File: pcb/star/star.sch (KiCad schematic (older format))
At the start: 20 parts, among them U1 AP2112K-3.3, U2 74AHC595, U3 74AHC595

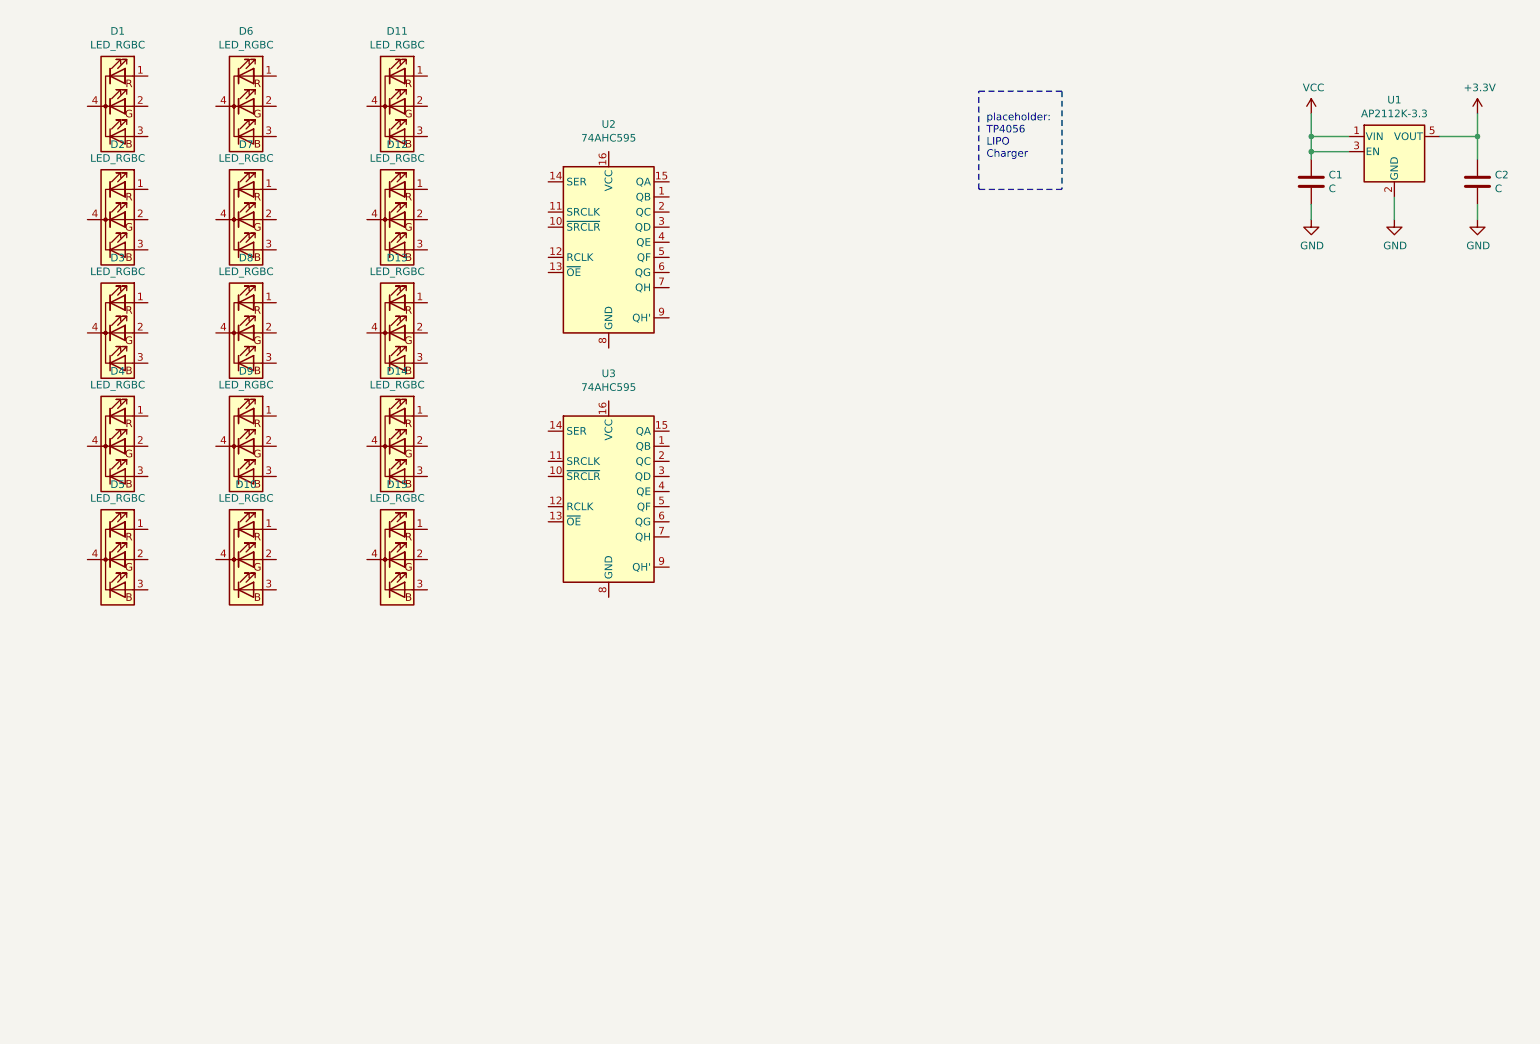
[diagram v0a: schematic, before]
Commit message: apa106 and esp12f used
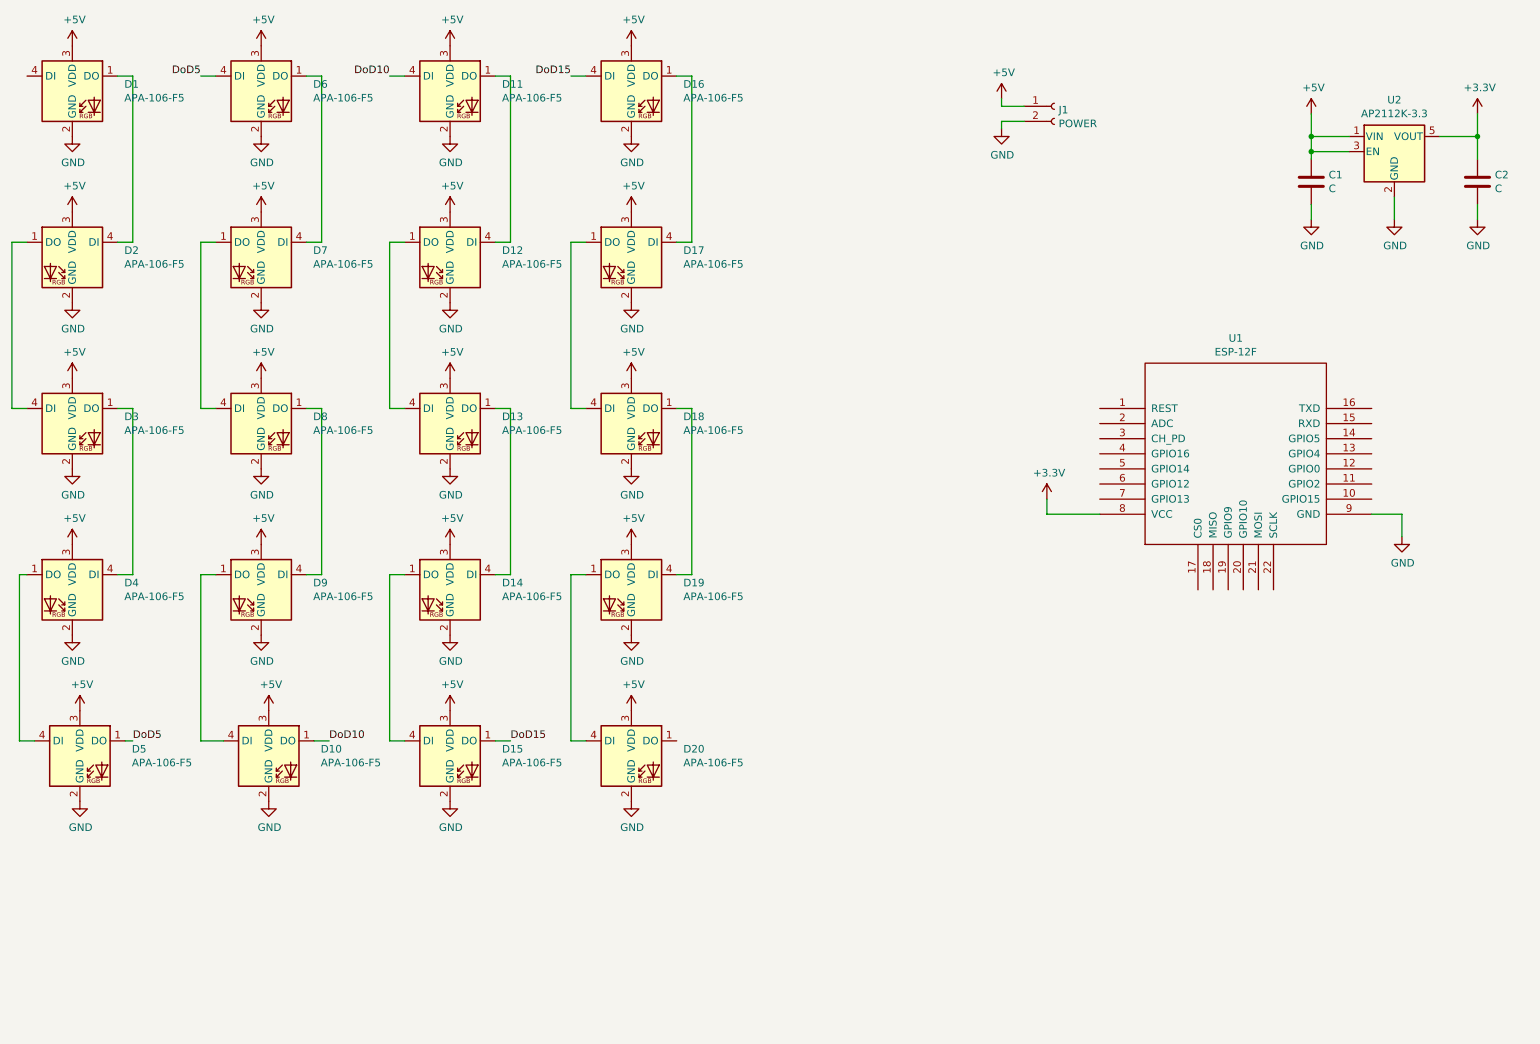
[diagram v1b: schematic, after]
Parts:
- removed D1, D10, D11, D12, D13, D14, D15, D2, D3, D4, D5, D6, D7, D8, D9: LED_RGBC, LED_THT:LED_D5.0mm-4_RGB, symbol Device:LED_RGBC
- removed U2, U3: 74AHC595, Package_SO:SOIC-16_3.9x9.9mm_P1.27mm, symbol 74xx:74AHC595
- added D1, D10, D11, D12, D13, D14, D15, D16, D17, D18, D19, D2, D20, D3, D4, D5, D6, D7, D8, D9: APA-106-F5, LED_THT:LED_D5.0mm-4_RGB, symbol LED:APA-106-F5
- added J1: POWER, Connector_PinSocket_2.54mm:PinSocket_1x02_P2.54mm_Vertical, symbol Connector:Conn_01x02_Female
- added U1: ESP-12F, ESP8266:ESP-12E_SMD, symbol ESP8266:ESP-12F
- renumbered U1 to U2
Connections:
- net +3V3: now also U1.8 (VCC)
- net GND: now also D1.2 (GND), D10.2 (GND), D11.2 (GND), D12.2 (GND), D13.2 (GND), D14.2 (GND), D15.2 (GND), D16.2 (GND), D17.2 (GND), D18.2 (GND), D19.2 (GND), D2.2 (GND), D20.2 (GND), D3.2 (GND), D4.2 (GND), D5.2 (GND), D6.2 (GND), D7.2 (GND), D8.2 (GND), D9.2 (GND), J1.2 (Pin_2), U1.9 (GND)
- net VCC renamed +5V
- net +5V: now also D1.3 (VDD), D10.3 (VDD), D11.3 (VDD), D12.3 (VDD), D13.3 (VDD), D14.3 (VDD), D15.3 (VDD), D16.3 (VDD), D17.3 (VDD), D18.3 (VDD), D19.3 (VDD), D2.3 (VDD), D20.3 (VDD), D3.3 (VDD), D4.3 (VDD), D5.3 (VDD), D6.3 (VDD), D7.3 (VDD), D8.3 (VDD), D9.3 (VDD), J1.1 (Pin_1)
- new net: D1.1 (DO), D2.4 (DI)
- new net: D2.1 (DO), D3.4 (DI)
- new net: D3.1 (DO), D4.4 (DI)
- new net: D4.1 (DO), D5.4 (DI)
- new net: D6.1 (DO), D7.4 (DI)
- new net: D7.1 (DO), D8.4 (DI)
- new net: D8.1 (DO), D9.4 (DI)
- new net: D10.4 (DI), D9.1 (DO)
- new net: D11.1 (DO), D12.4 (DI)
- new net: D12.1 (DO), D13.4 (DI)
- new net: D13.1 (DO), D14.4 (DI)
- new net: D14.1 (DO), D15.4 (DI)
- new net: D16.1 (DO), D17.4 (DI)
- new net: D17.1 (DO), D18.4 (DI)
- new net: D18.1 (DO), D19.4 (DI)
- new net: D19.1 (DO), D20.4 (DI)
- new net DoD10: D10.1 (DO), D11.4 (DI)
- new net DoD15: D15.1 (DO), D16.4 (DI)
- new net DoD5: D5.1 (DO), D6.4 (DI)
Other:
- note removed: "placeholder:\nTP4056\nLIPO \nCharger"

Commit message: layout first pass done
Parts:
- added C3, C4, C5: 100nF, Capacitor_THT:C_Disc_D5.0mm_W2.5mm_P2.50mm, symbol Device:C
- added J2: Conn_01x06_Male, symbol Connector:Conn_01x06_Male
- added R1, R2, R3: 10k, Resistor_THT:R_Axial_DIN0204_L3.6mm_D1.6mm_P7.62mm_Horizontal, symbol Device:R
- added SW1: RST, Button_Switch_SMD:SW_SPST_EVQPE1, symbol Switch:SW_Push
- added SW2: PRG, Button_Switch_SMD:SW_SPST_EVQPE1, symbol Switch:SW_Push
- C1: value C -> 10uF; footprint (none) -> Capacitor_THT:CP_Radial_D5.0mm_P2.50mm
- C2: value C -> 1uF; footprint (none) -> Capacitor_THT:CP_Radial_D5.0mm_P2.50mm
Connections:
- net +3V3: now also J2.1 (Pin_1), R1.1, R2.1, R3.1
- net +5V: now also C3.1
- net GND: now also C3.2, C4.1, C5.1, J2.4 (Pin_4), SW1.2, SW2.2
- net RST: now reaches U1.1 (REST)
- net RST: now also C4.2, J2.6 (Pin_6), R2.2, SW1.1
- net GPIO0: now reaches U1.12 (GPIO0)
- net GPIO0: now also C5.2, J2.5 (Pin_5), R3.2, SW2.1
- net LED_Din: now reaches U1.14 (GPIO5)
- net LED_Din: now also D20.4 (DI)
- net RXD: now reaches U1.15 (RXD)
- net RXD: now also J2.3 (Pin_3)
- net TXD: now reaches U1.16 (TXD)
- net TXD: now also J2.2 (Pin_2)
- net ADC: now reaches U1.2 (ADC)
- net at U1.3 (CH_PD): now also R1.2
- net at D1.4 (DI): now also D20.1 (DO)
- net at D19.1 (DO): no longer D20.4 (DI)
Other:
- moved on the sheet: C2, D1, D10, D11, D12, D13, D14, D15, D16, D17, D18, D19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

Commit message: routing second pass
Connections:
- net ADC: no longer names the net of U1.2 (ADC)
- no-connect marks 0 -> 14
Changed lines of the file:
@@
 Wire Wire Line
 	6350 1750 6350 1650
-Text Label 6600 2200 2    50   ~ 0
-ADC
-Wire Wire Line
-	6600 2200 6650 2200
 Text Label 8550 2500 0    50   ~ 0
 GPIO0
@@
 Wire Wire Line
 	850  2200 950  2200
+NoConn ~ 6650 2200
+NoConn ~ 6650 2400
+NoConn ~ 6650 2500
+NoConn ~ 6650 2600
+NoConn ~ 6650 2700
+NoConn ~ 8450 2700
+NoConn ~ 8450 2600
+NoConn ~ 8450 2400
+NoConn ~ 7300 3300
+NoConn ~ 7400 3300
+NoConn ~ 7500 3300
+NoConn ~ 7600 3300
+NoConn ~ 7700 3300
+NoConn ~ 7800 3300
 $EndSCHEMATC
